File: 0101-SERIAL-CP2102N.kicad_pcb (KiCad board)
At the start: 2 copper layers, 19.6 x 19.6 mm, 2 parts

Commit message: Done PCB
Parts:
- added C1: 4.7uF, Capacitor_SMD:C_0402_1005Metric, B.Cu at (104.5, 108.5)
- added C2: 4.7uF, Capacitor_SMD:C_0402_1005Metric, B.Cu at (110.0, 105.0)
- added C3: 0.1uF, Capacitor_SMD:C_0402_1005Metric, B.Cu at (104.5, 109.5)
- added C4: 0.1uF, Capacitor_SMD:C_0402_1005Metric, B.Cu at (109.0, 105.0)
- added D1: LED_YEL, LED_SMD:LED_0603_1608Metric, F.Cu at (117.5, 118.0)
- added D10: LESD5Z5.0CT1G, Diode_SMD:D_SOD-523, F.Cu at (118.8, 105.5)
- added D11: LESD5Z5.0CT1G, Diode_SMD:D_SOD-523, F.Cu at (110.6, 112.5)
- added D2: LED_YEL, LED_SMD:LED_0603_1608Metric, F.Cu at (113.5, 118.0)
- added D3: LED_BLU, LED_SMD:LED_0603_1608Metric, F.Cu at (113.5, 102.0)
- added D4: LED_RED, LED_SMD:LED_0603_1608Metric, F.Cu at (117.5, 102.0)
- added D5: LESD5Z5.0CT1G, Diode_SMD:D_SOD-523, F.Cu at (110.6, 107.5)
- added D6: LESD5Z5.0CT1G, Diode_SMD:D_SOD-523, F.Cu at (110.6, 110.0)
- added D7: LESD5Z5.0CT1G, Diode_SMD:D_SOD-523, F.Cu at (118.8, 114.5)
- added D8: LESD5Z5.0CT1G, Diode_SMD:D_SOD-523, F.Cu at (110.6, 115.6)
- added D9: LESD5Z5.0CT1G, Diode_SMD:D_SOD-523, F.Cu at (110.6, 104.9)
- added J1: USB-C, JLC-SMT:HRO_TYPE-C-31-M-12, F.Cu at (104.0, 110.0)
- added J2: Conn_02x04_Odd_Even, Connector_PinHeader_2.54mm:PinHeader_2x04_P2.54mm_Vertical, F.Cu at (113.7, 106.2)
- added Q1: DDC114TH, Package_TO_SOT_SMD:SOT-363_SC-70-6, B.Cu at (105.0, 117.5)
- added R1: 22.1K, Resistor_SMD:R_0402_1005Metric, B.Cu at (111.0, 105.0)
- added R12: 1.5K, Resistor_SMD:R_0402_1005Metric, F.Cu at (116.2, 117.5)
- added R13: 1.5K, Resistor_SMD:R_0402_1005Metric, F.Cu at (112.2, 117.5)
- added R14: 1.5K, Resistor_SMD:R_0402_1005Metric, F.Cu at (112.2, 102.5)
- added R15: 1.5K, Resistor_SMD:R_0402_1005Metric, F.Cu at (116.2, 102.5)
- added R2: 47.5K, Resistor_SMD:R_0402_1005Metric, B.Cu at (112.0, 105.0)
- added R3: 1K, Resistor_SMD:R_0402_1005Metric, B.Cu at (104.5, 107.5)
- added R4: 5.1K, Resistor_SMD:R_0402_1005Metric, F.Cu at (110.5, 108.8)
- added R5: 5.1K, Resistor_SMD:R_0402_1005Metric, F.Cu at (110.5, 111.2)
- added R8: 0R(NC), Resistor_SMD:R_0603_1608Metric, B.Cu at (107.5, 117.5)
- added R9: 0R(NC), Resistor_SMD:R_0603_1608Metric, B.Cu at (102.5, 117.5)
- added U1: CP2102N-A02-GQFN24, Package_DFN_QFN:QFN-24-1EP_4x4mm_P0.5mm_EP2.6x2.6mm, B.Cu at (110.0, 110.0)
- added kibuzzard-63353A29: G***, kibuzzard-63353A29, F.Cu at (115.0, 102.0)
- added kibuzzard-63353A37: G***, kibuzzard-63353A37, F.Cu at (119.0, 102.0)
- added kibuzzard-63395349: G***, kibuzzard-63395349, F.Cu at (115.0, 118.0)
- added kibuzzard-6339534D: G***, kibuzzard-6339534D, F.Cu at (119.0, 118.0)
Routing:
- net VDD: track 0.00 -> 45.4 mm, vias 0 -> 8
- net /RTS/BOOT: track 0.00 -> 38.9 mm, vias 0 -> 2
- net /DTR/RESET: track 0.00 -> 30.7 mm
- net /RTS: track 0.00 -> 14.7 mm, vias 0 -> 2
- net /TXD: track 0.00 -> 14.6 mm
- net Net-(R3-Pad2): track 0.00 -> 13.9 mm, vias 0 -> 2
- net /CTS: track 0.00 -> 11.1 mm
- net /RXD: track 0.00 -> 10.7 mm
- net /DTR: track 0.00 -> 9.74 mm
- net /D+: track 0.00 -> 6.16 mm, vias 0 -> 1
- net Net-(R1-Pad2): track 0.00 -> 6.01 mm
- net /D-: track 0.00 -> 5.21 mm, vias 0 -> 1
- net GND: track 0.00 -> 3.87 mm, vias 0 -> 35
- net VBUS: track 0.00 -> 2.94 mm, vias 0 -> 6
- net Net-(J1-PadB5): track 0.00 -> 2.16 mm
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- added copper zone on B.Cu, net GND
- added copper zone on F.Cu, net GND
- added copper zone on In1.Cu, net GND
- added copper zone on In2.Cu, net GND
- added copper zone on B.Cu, net VBUS
- added copper zone on F.Cu, net VBUS
- added copper zone on In1.Cu, net VBUS
- added copper zone on In2.Cu, net VBUS
- added copper zone on B.Cu, net VDD
- added copper zone on In1.Cu, net VDD
- removed copper zone on B.Cu, net (none)
- removed copper zone on F.Cu, net (none)
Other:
- outline, holes or cut-outs redrawn
- copper layers 2 -> 4
- board text added: "3"
- board text added: "5"
- board text added: "CP2102N"
- board text added: "CTS"
- board text added: "GND"
- board text removed: "TEMPLATE"

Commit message: Finish BOM
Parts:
- Q1: value DDC114TH -> PUMH4,115

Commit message: Finish silks
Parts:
- added kibuzzard-633A4DBF: G***, kibuzzard-633A4DBF, B.Cu at (114.2, 117.8)
- added kibuzzard-633A4E09: G***, kibuzzard-633A4E09, B.Cu at (104.0, 113.0)
- moved R8 0.15 mm to (107.3, 117.5)
- moved R9 0.15 mm to (102.7, 117.5)

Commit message: Adjust position of LEDs
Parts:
- moved D1 0.25 mm to (117.2, 118.0)
- moved D2 0.25 mm to (113.2, 118.0)
- moved D3 0.25 mm to (113.2, 102.0)
- moved D4 0.25 mm to (117.2, 102.0)
- moved R12 0.25 mm to (116.0, 117.5)
- moved R13 0.25 mm to (112.0, 117.5)
- moved R14 0.25 mm to (112.0, 102.5)
- moved R15 0.25 mm to (116.0, 102.5)
- moved kibuzzard-63353A29 0.25 mm to (114.8, 102.0)
- moved kibuzzard-63353A37 0.25 mm to (118.8, 102.0)
- moved kibuzzard-63395349 0.25 mm to (114.8, 118.0)
- moved kibuzzard-6339534D 0.25 mm to (118.8, 118.0)
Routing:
- net VDD: track 45.4 -> 44.9 mm
- net GND: vias 35 -> 34

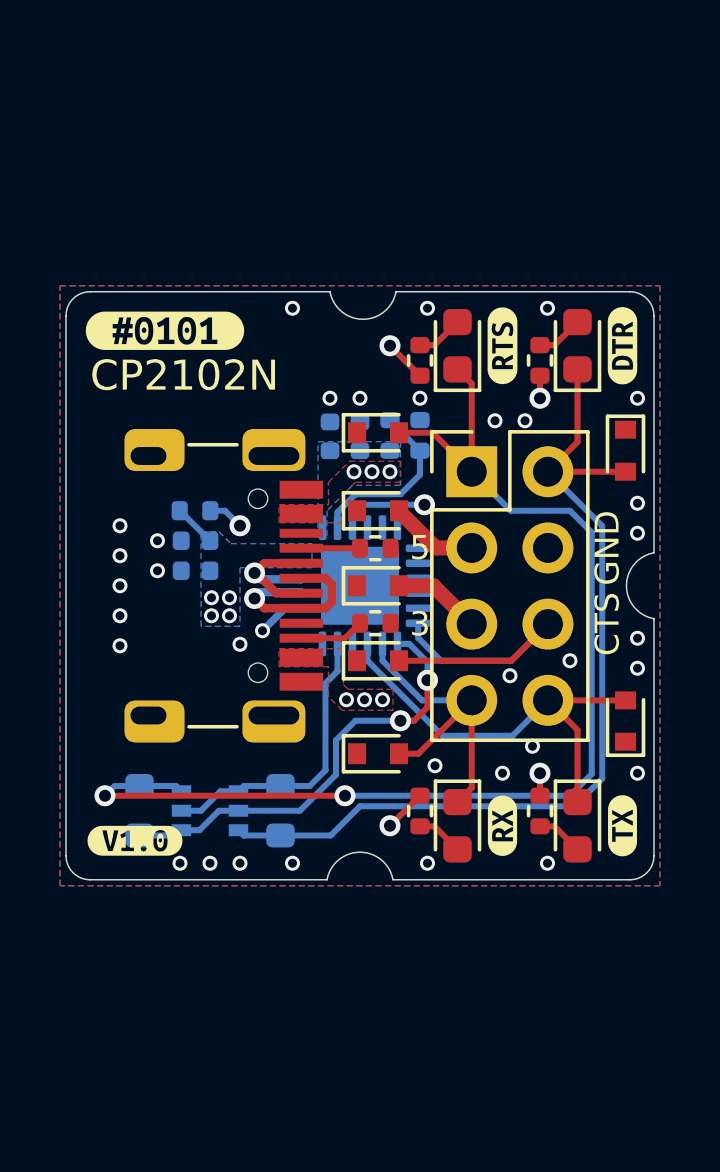
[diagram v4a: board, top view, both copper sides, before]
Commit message: Add craft edge
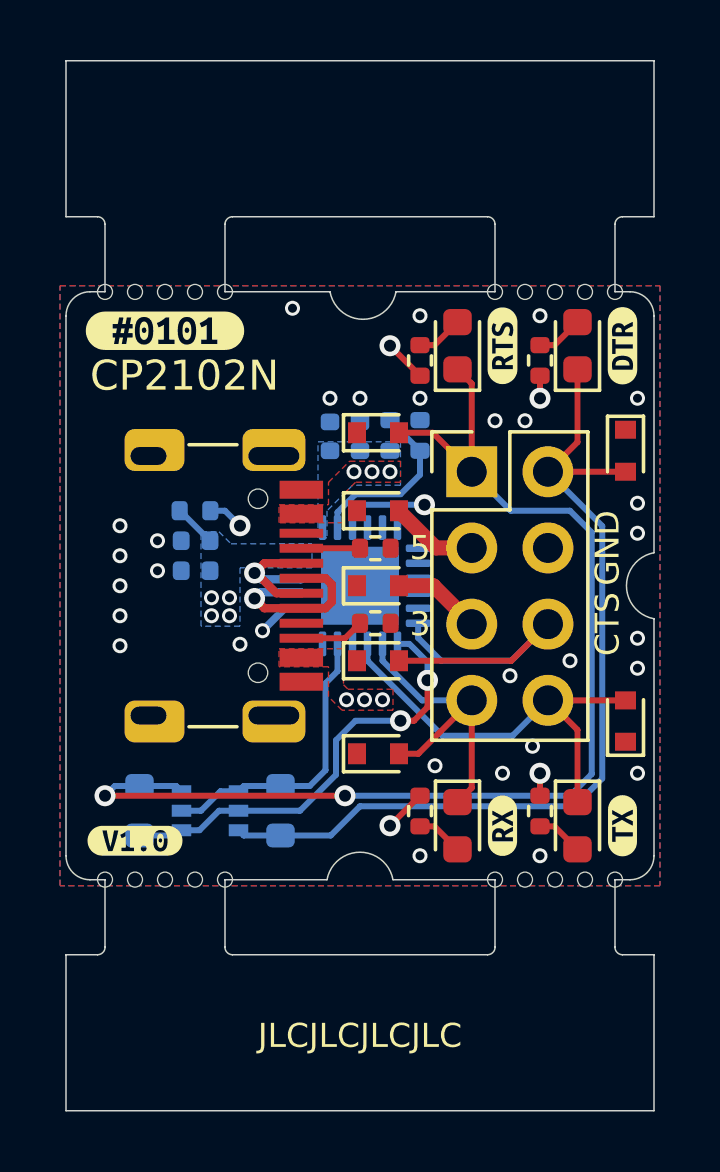
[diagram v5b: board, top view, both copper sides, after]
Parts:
- added REF**: JLC_CRAFT_EDGE, JLC-SMT:JLC_CRAFT_EDGE_3P, F.Cu at (116.5, 119.8)
- added REF**: JLC_CRAFT_EDGE, JLC-SMT:JLC_CRAFT_EDGE_3P, F.Cu at (103.5, 119.8)
- added REF**: JLC_CRAFT_EDGE, JLC-SMT:JLC_CRAFT_EDGE_3P, F.Cu at (103.5, 100.2)
- added REF**: JLC_CRAFT_EDGE, JLC-SMT:JLC_CRAFT_EDGE_3P, F.Cu at (116.5, 100.2)
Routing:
- net GND: vias 34 -> 30
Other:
- board size 19.6 x 19.6 mm -> 19.6 x 35 mm
- board text added: "JLCJLCJLCJLC"
